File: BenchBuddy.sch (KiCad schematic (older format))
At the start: 0 parts

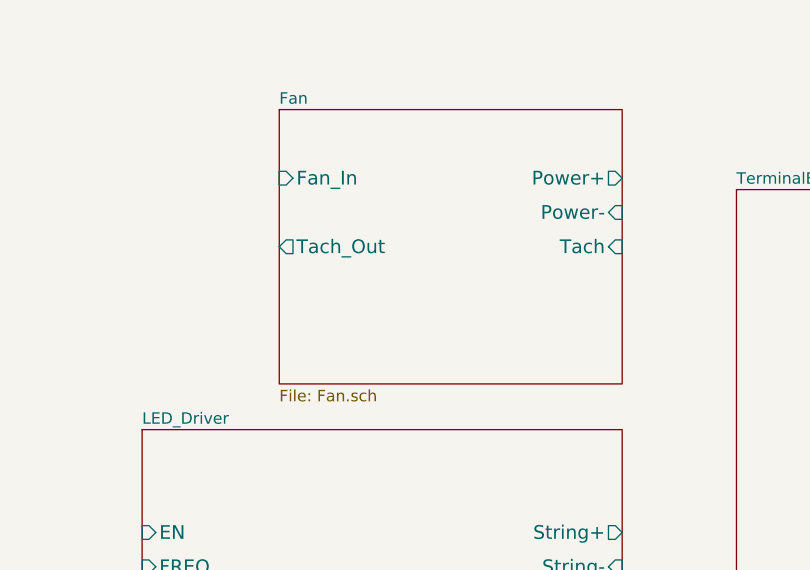
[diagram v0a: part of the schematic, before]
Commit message: Fan Schematic
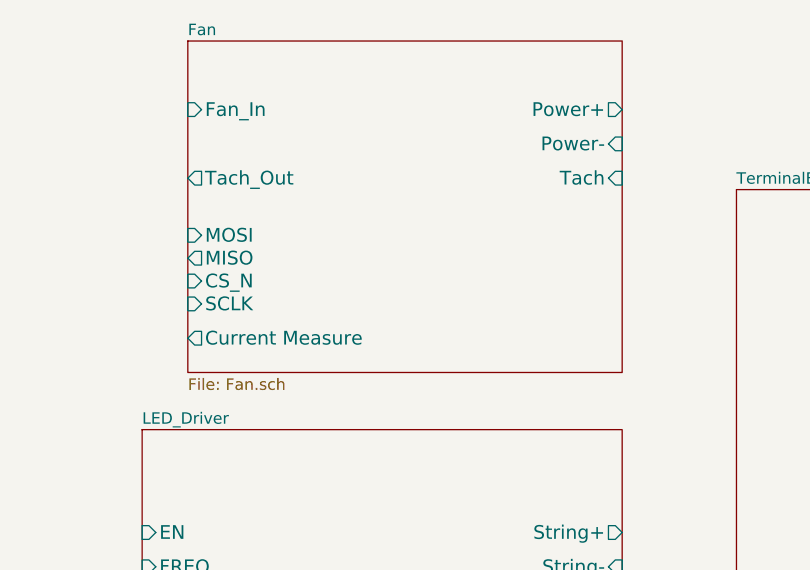
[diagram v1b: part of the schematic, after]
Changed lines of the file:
@@
 Sheet 1 8
 Title ""
-Date "19 sep 2013"
+Date "20 sep 2013"
 Rev ""
 Comp ""
@@
 $EndSheet
 $Sheet
-S 8250 1100 1500 1200
+S 7850 800  1900 1450
 U 5237E1FA
 F0 "Fan" 50
 F1 "Fan.sch" 50
-F2 "Fan_In" I L 8250 1400 60
-F3 "Tach_Out" O L 8250 1700 60
-F4 "Power+" O R 9750 1400 60
-F5 "Power-" I R 9750 1550 60
-F6 "Tach" I R 9750 1700 60
+F2 "Fan_In" I L 7850 1100 60
+F3 "Tach_Out" O L 7850 1400 60
+F4 "Power+" O R 9750 1100 60
+F5 "Power-" I R 9750 1250 60
+F6 "Tach" I R 9750 1400 60
+F7 "MOSI" I L 7850 1650 60
+F8 "MISO" O L 7850 1750 60
+F9 "CS_N" I L 7850 1850 60
+F10 "SCLK" I L 7850 1950 60
+F11 "Current Measure" O L 7850 2100 60
 $EndSheet
 $Sheet

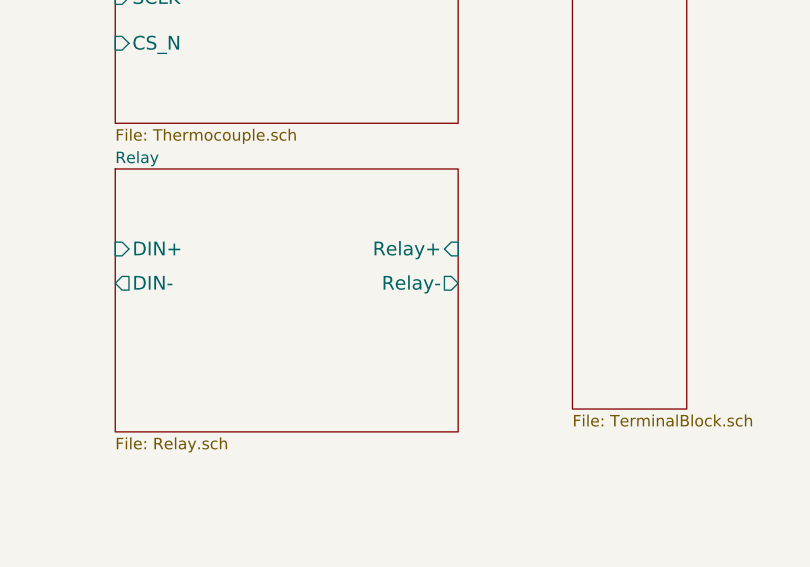
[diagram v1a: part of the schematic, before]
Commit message: Relay Schematic
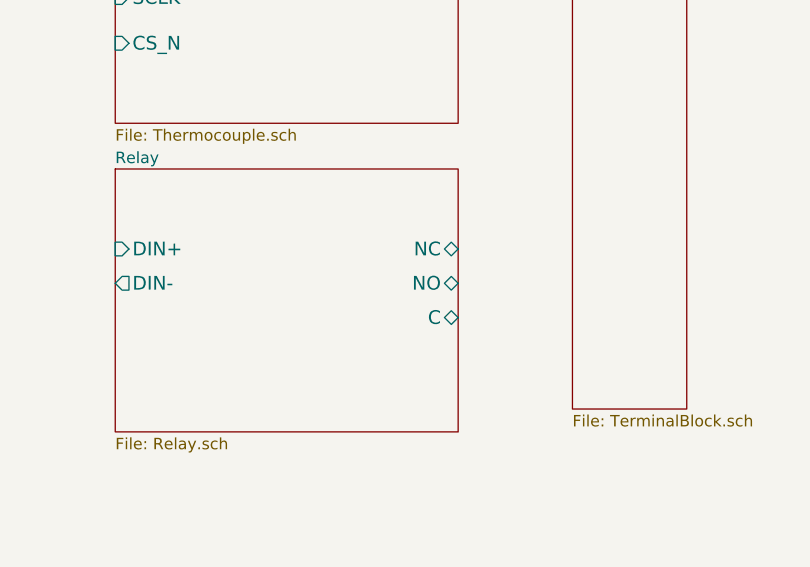
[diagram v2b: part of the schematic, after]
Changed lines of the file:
@@
 LIBS:contrib
 LIBS:valves
+LIBS:BenchBuddy
 LIBS:BenchBuddy-cache
 EELAYER 27 0
@@
 Sheet 1 8
 Title ""
-Date "20 sep 2013"
+Date "21 sep 2013"
 Rev ""
 Comp ""
@@
 F6 "SCLK" I L 8250 4950 60
 F7 "CS_N" I L 8250 5150 60
-$EndSheet
-$Sheet
-S 8250 5700 1500 1150
-U 5237E13C
-F0 "Relay" 50
-F1 "Relay.sch" 50
-F2 "DIN+" I L 8250 6050 60
-F3 "DIN-" O L 8250 6200 60
-F4 "Relay+" I R 9750 6050 60
-F5 "Relay-" O R 9750 6200 60
 $EndSheet
 $Sheet
@@
 F1 "TerminalBlock.sch" 50
 $EndSheet
+$Sheet
+S 8250 5700 1500 1150
+U 5237E13C
+F0 "Relay" 50
+F1 "Relay.sch" 50
+F2 "DIN+" I L 8250 6050 60
+F3 "DIN-" O L 8250 6200 60
+F6 "NC" B R 9750 6050 60
+F7 "NO" B R 9750 6200 60
+F8 "C" B R 9750 6350 60
+$EndSheet
 $EndSCHEMATC

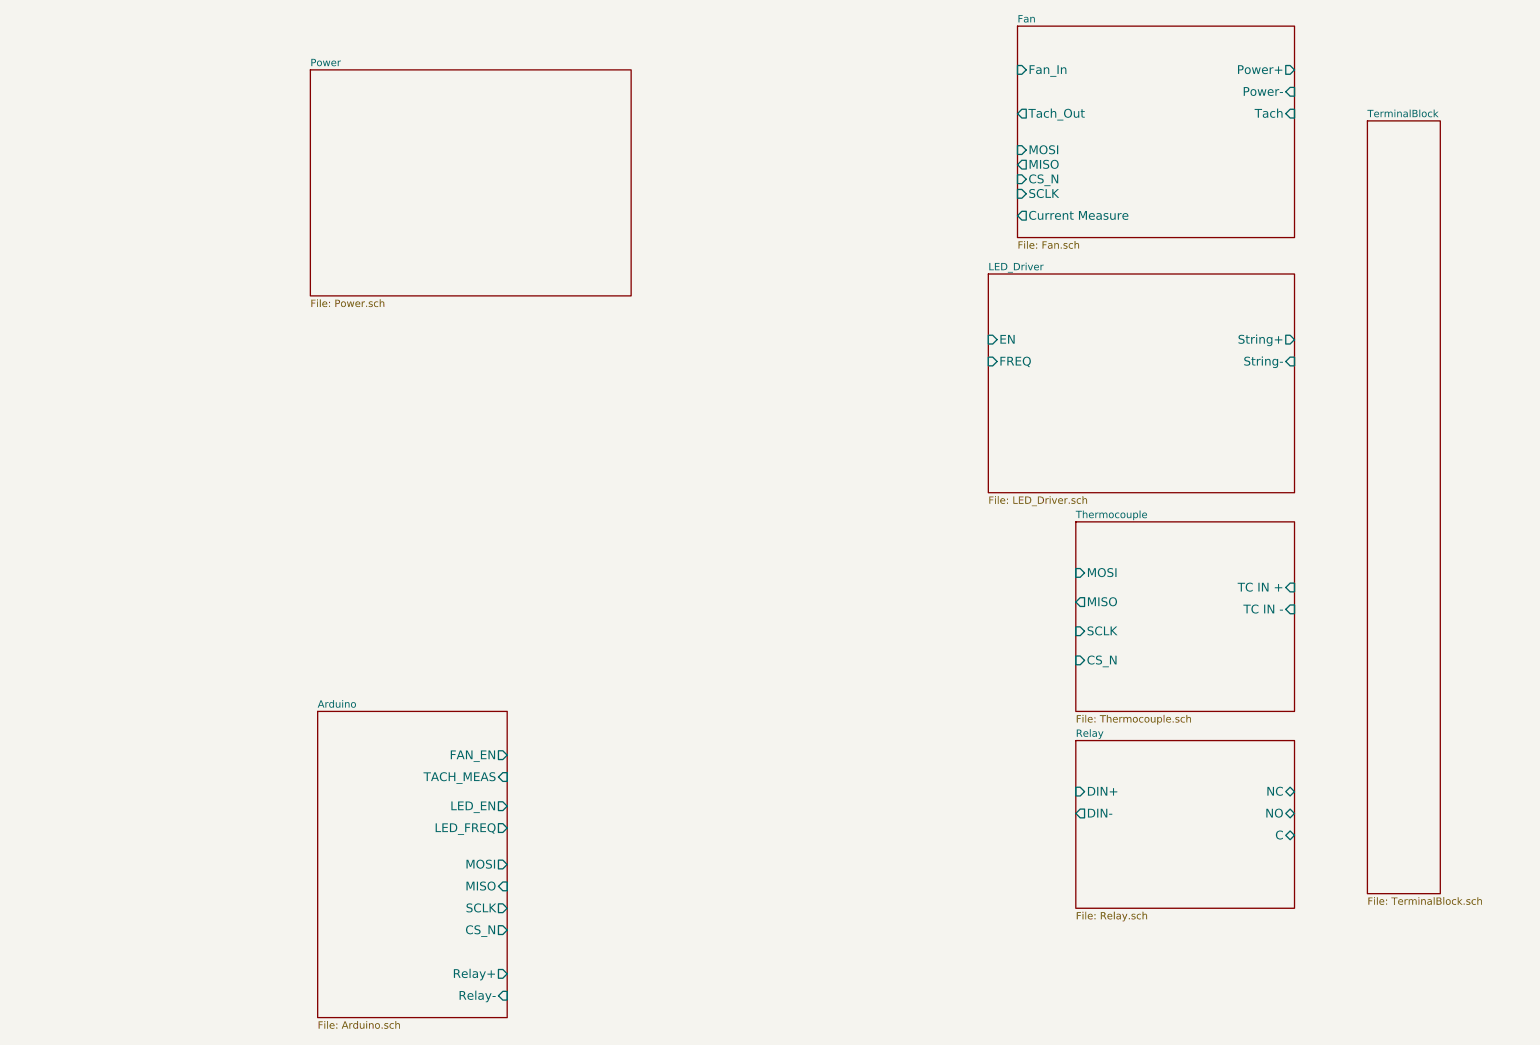
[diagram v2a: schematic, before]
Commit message: Power Protection And Filtering
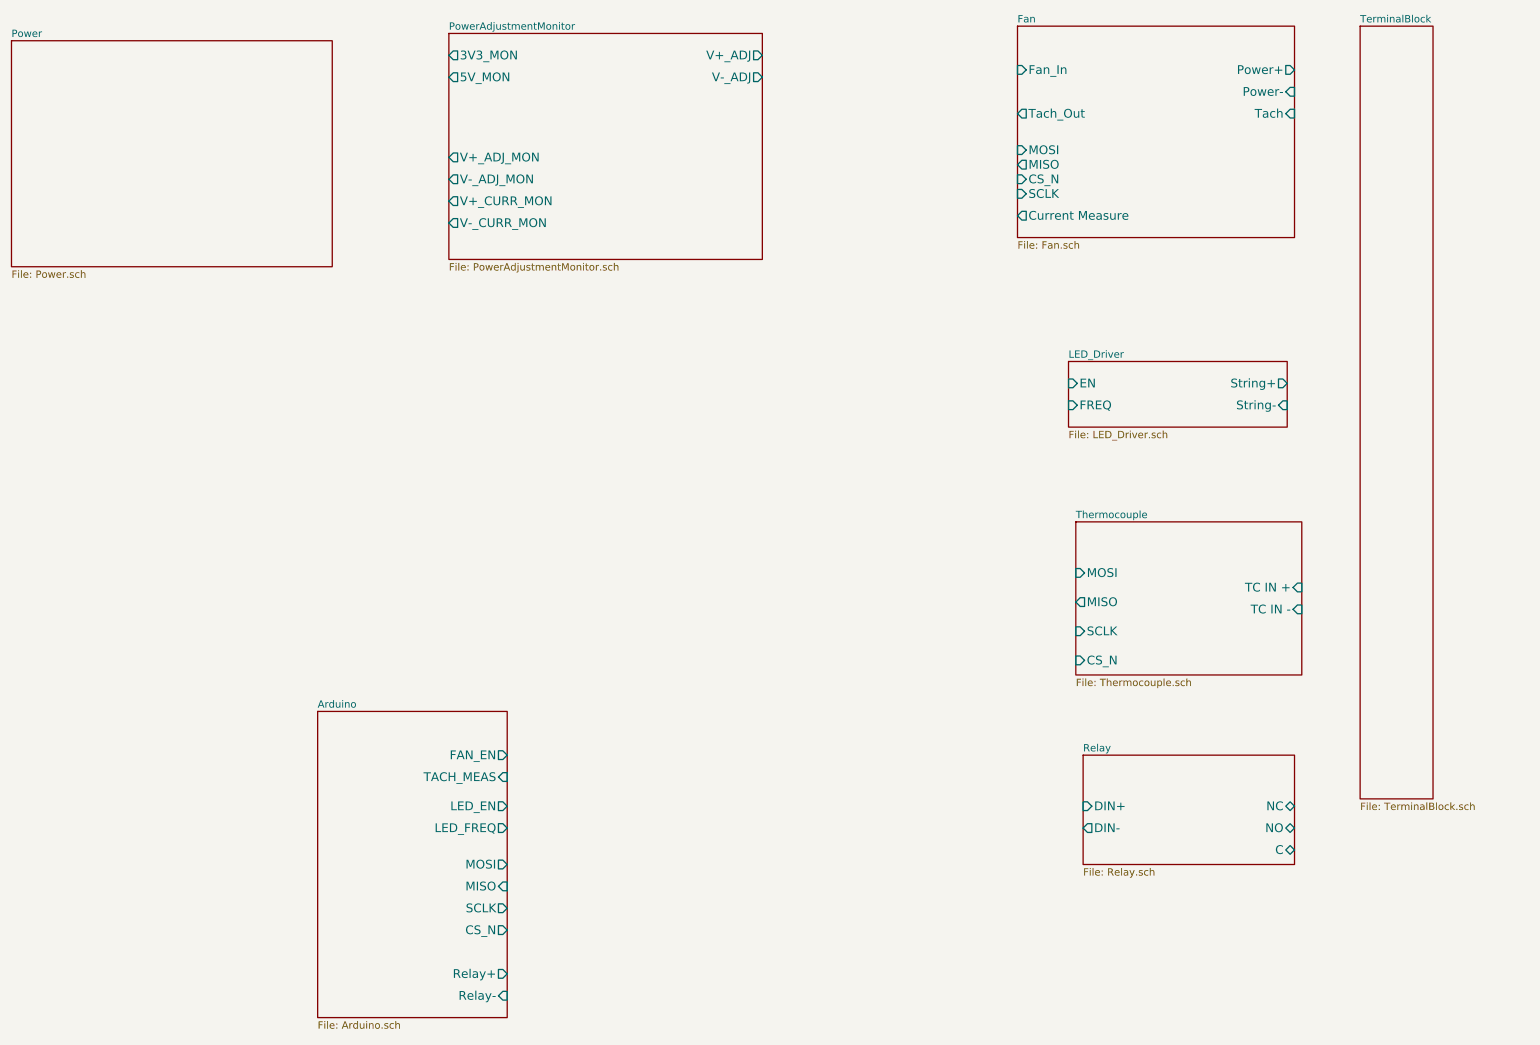
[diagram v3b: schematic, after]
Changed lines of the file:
@@
 $Descr A4 11693 8268
 encoding utf-8
-Sheet 1 8
+Sheet 1 9
 Title ""
-Date "21 sep 2013"
+Date "22 sep 2013"
 Rev ""
 Comp ""
@@
 $EndSheet
 $Sheet
-S 8250 4200 1500 1300
+S 8250 4200 1550 1050
 U 5237E11D
 F0 "Thermocouple" 50
 F1 "Thermocouple.sch" 50
-F2 "TC IN +" I R 9750 4650 60
-F3 "TC IN -" I R 9750 4800 60
+F2 "TC IN +" I R 9800 4650 60
+F3 "TC IN -" I R 9800 4800 60
 F4 "MOSI" I L 8250 4550 60
 F5 "MISO" O L 8250 4750 60
@@
 $EndSheet
 $Sheet
-S 3000 1100 2200 1550
+S 950  900  2200 1550
 U 5237E175
 F0 "Power" 50
@@
 $EndSheet
 $Sheet
-S 7650 2500 2100 1500
+S 8200 3100 1500 450
 U 5237E1C9
 F0 "LED_Driver" 50
 F1 "LED_Driver.sch" 50
-F2 "EN" I L 7650 2950 60
-F3 "FREQ" I L 7650 3100 60
-F4 "String+" O R 9750 2950 60
-F5 "String-" I R 9750 3100 60
+F2 "EN" I L 8200 3250 60
+F3 "FREQ" I L 8200 3400 60
+F4 "String+" O R 9700 3250 60
+F5 "String-" I R 9700 3400 60
 $EndSheet
 $Sheet
@@
 $EndSheet
 $Sheet
-S 10250 1450 500  5300
+S 10200 800  500  5300
 U 5237E269
 F0 "TerminalBlock" 50
@@
 $EndSheet
 $Sheet
-S 8250 5700 1500 1150
+S 8300 5800 1450 750
 U 5237E13C
 F0 "Relay" 50
 F1 "Relay.sch" 50
-F2 "DIN+" I L 8250 6050 60
-F3 "DIN-" O L 8250 6200 60
-F6 "NC" B R 9750 6050 60
-F7 "NO" B R 9750 6200 60
-F8 "C" B R 9750 6350 60
+F2 "DIN+" I L 8300 6150 60
+F3 "DIN-" O L 8300 6300 60
+F4 "NC" B R 9750 6150 60
+F5 "NO" B R 9750 6300 60
+F6 "C" B R 9750 6450 60
+$EndSheet
+$Sheet
+S 3950 850  2150 1550
+U 523E68DB
+F0 "PowerAdjustmentMonitor" 50
+F1 "PowerAdjustmentMonitor.sch" 50
+F2 "V+_ADJ" O R 6100 1000 60
+F3 "V-_ADJ" O R 6100 1150 60
+F4 "3V3_MON" O L 3950 1000 60
+F5 "5V_MON" O L 3950 1150 60
+F6 "V+_ADJ_MON" O L 3950 1700 60
+F7 "V-_ADJ_MON" O L 3950 1850 60
+F8 "V+_CURR_MON" O L 3950 2000 60
+F9 "V-_CURR_MON" O L 3950 2150 60
 $EndSheet
 $EndSCHEMATC

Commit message: Overall Schematic
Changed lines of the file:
@@
 Sheet 1 9
 Title ""
-Date "22 sep 2013"
+Date "28 sep 2013"
 Rev ""
 Comp ""
@@
 $EndDescr
 $Sheet
-S 3050 5500 1300 2100
-U 5237E014
-F0 "Arduino" 50
-F1 "Arduino.sch" 50
-F2 "FAN_EN" O R 4350 5800 60
-F3 "TACH_MEAS" I R 4350 5950 60
-F4 "LED_EN" O R 4350 6150 60
-F5 "LED_FREQ" O R 4350 6300 60
-F6 "MOSI" O R 4350 6550 60
-F7 "MISO" I R 4350 6700 60
-F8 "SCLK" O R 4350 6850 60
-F9 "CS_N" O R 4350 7000 60
-F10 "Relay+" O R 4350 7300 60
-F11 "Relay-" I R 4350 7450 60
-$EndSheet
-$Sheet
-S 8250 4200 1550 1050
+S 8200 2950 1550 1050
 U 5237E11D
 F0 "Thermocouple" 50
 F1 "Thermocouple.sch" 50
-F2 "TC IN +" I R 9800 4650 60
-F3 "TC IN -" I R 9800 4800 60
-F4 "MOSI" I L 8250 4550 60
-F5 "MISO" O L 8250 4750 60
-F6 "SCLK" I L 8250 4950 60
-F7 "CS_N" I L 8250 5150 60
+F2 "TC IN +" I R 9750 3400 60
+F3 "TC IN -" I R 9750 3550 60
+F4 "MOSI" I L 8200 3300 60
+F5 "MISO" O L 8200 3400 60
+F6 "SCLK" I L 8200 3500 60
+F7 "CS_N" I L 8200 3600 60
 $EndSheet
 $Sheet
@@
 $EndSheet
 $Sheet
-S 8200 3100 1500 450
+S 8250 4400 1500 450
 U 5237E1C9
 F0 "LED_Driver" 50
 F1 "LED_Driver.sch" 50
-F2 "EN" I L 8200 3250 60
-F3 "FREQ" I L 8200 3400 60
-F4 "String+" O R 9700 3250 60
-F5 "String-" I R 9700 3400 60
-$EndSheet
-$Sheet
-S 7850 800  1900 1450
+F2 "LED_EN_PWM" I L 8250 4600 60
+F3 "LED_STRING+" O R 9750 4550 60
+F4 "LED_STRING-" O R 9750 4700 60
+$EndSheet
+$Sheet
+S 7850 1100 1900 1450
 U 5237E1FA
 F0 "Fan" 50
 F1 "Fan.sch" 50
-F2 "Fan_In" I L 7850 1100 60
-F3 "Tach_Out" O L 7850 1400 60
-F4 "Power+" O R 9750 1100 60
-F5 "Power-" I R 9750 1250 60
-F6 "Tach" I R 9750 1400 60
-F7 "MOSI" I L 7850 1650 60
-F8 "MISO" O L 7850 1750 60
-F9 "CS_N" I L 7850 1850 60
-F10 "SCLK" I L 7850 1950 60
-F11 "Current Measure" O L 7850 2100 60
-$EndSheet
-$Sheet
-S 10200 800  500  5300
+F2 "MOSI" I L 7850 1550 60
+F3 "MISO" O L 7850 1650 60
+F4 "CS_N" I L 7850 1750 60
+F5 "SCLK" I L 7850 1850 60
+F6 "FAN_EN_N" I L 7850 1250 60
+F7 "TACH_MEAS" O L 7850 2200 60
+F8 "FAN_OUT+" O R 9750 1350 60
+F9 "FAN_OUT-" O R 9750 1500 60
+F10 "TACH_IN" I R 9750 2300 60
+F11 "CURR_MEAS" O L 7850 2300 60
+$EndSheet
+$Sheet
+S 8250 5550 1450 750
+U 5237E13C
+F0 "Relay" 50
+F1 "Relay.sch" 50
+F2 "RELAY+" I L 8250 5800 60
+F3 "RELAY-" O L 8250 6000 60
+F4 "RELAY_NC" B R 9700 5900 60
+F5 "RELAY_NO" B R 9700 5800 60
+F6 "RELAY_COM" B R 9700 5700 60
+$EndSheet
+$Sheet
+S 4950 800  2050 1450
+U 523E68DB
+F0 "PowerAdjustmentMonitor" 50
+F1 "PowerAdjustmentMonitor.sch" 50
+F2 "V+_ADJ" O R 7000 900 60
+F3 "V-_ADJ" O R 7000 1000 60
+F4 "3V3_MON" O L 4950 950 60
+F5 "5V_MON" O L 4950 1100 60
+F6 "V+_ADJ_MON" O L 4950 1950 60
+F7 "V-_ADJ_MON" O L 4950 2100 60
+F8 "V+_CURR_MON" O L 4950 1350 60
+F9 "V-_CURR_MON" O L 4950 1500 60
+$EndSheet
+Wire Wire Line
+	4050 4100 4400 4100
+Wire Wire Line
+	4400 4100 4400 1950
+Wire Wire Line
+	4400 1950 4950 1950
+Wire Wire Line
+	4950 2100 4500 2100
+Wire Wire Line
+	4500 2100 4500 4200
+Wire Wire Line
+	4500 4200 4050 4200
+Wire Wire Line
+	4050 4350 7150 4350
+Wire Wire Line
+	7150 4350 7150 1250
+Wire Wire Line
+	7150 1250 7850 1250
+Wire Wire Line
+	7850 1550 7200 1550
+Wire Wire Line
+	7200 1550 7200 4500
+Wire Wire Line
+	7200 4500 4050 4500
+Wire Wire Line
+	4050 4600 7250 4600
+Wire Wire Line
+	7250 4600 7250 1650
+Wire Wire Line
+	7250 1650 7850 1650
+Wire Wire Line
+	7850 1750 7300 1750
+Wire Wire Line
+	7300 1750 7300 4700
+Wire Wire Line
+	7300 4700 4050 4700
+Wire Wire Line
+	4050 4800 7350 4800
+Wire Wire Line
+	7350 4800 7350 1850
+Wire Wire Line
+	7350 1850 7850 1850
+Wire Wire Line
+	7850 2200 7400 2200
+Wire Wire Line
+	7400 2200 7400 4950
+Wire Wire Line
+	7400 4950 4050 4950
+Wire Wire Line
+	4050 5050 7450 5050
+Wire Wire Line
+	7450 5050 7450 2300
+Wire Wire Line
+	7450 2300 7850 2300
+Wire Wire Line
+	8200 3300 7200 3300
+Connection ~ 7200 3300
+Wire Wire Line
+	8200 3400 7250 3400
+Connection ~ 7250 3400
+$Sheet
+S 2750 4000 1300 2100
+U 5237E014
+F0 "Arduino" 50
+F1 "Arduino.sch" 50
+F2 "TACH_MEAS" I R 4050 4950 60
+F3 "MOSI" O R 4050 4500 60
+F4 "MISO" I R 4050 4600 60
+F5 "SCLK" O R 4050 4800 60
+F6 "FAN_EN_N" O R 4050 4350 60
+F7 "CURR_MEAS" I R 4050 5050 60
+F8 "RELAY+" O R 4050 5800 60
+F9 "RELAY-" O R 4050 6000 60
+F10 "V+_ADJ_MON" I R 4050 4100 60
+F11 "V-_ADJ_MON" I R 4050 4200 60
+F12 "LED_EN_PWM" O R 4050 5300 60
+F13 "DAC_CS_N" O R 4050 4700 60
+F14 "ADC_CS_N" O R 4050 5150 60
+$EndSheet
+Wire Wire Line
+	7350 3500 8200 3500
+Connection ~ 7350 3500
+Wire Wire Line
+	8200 3600 7500 3600
+Wire Wire Line
+	7500 3600 7500 5150
+Wire Wire Line
+	7500 5150 4050 5150
+Wire Wire Line
+	4050 5300 7700 5300
+Wire Wire Line
+	7700 5300 7700 4600
+Wire Wire Line
+	7700 4600 8250 4600
+Wire Wire Line
+	4050 5800 8250 5800
+Wire Wire Line
+	8250 6000 4050 6000
+$Sheet
+S 10250 800  750  5500
 U 5237E269
 F0 "TerminalBlock" 50
 F1 "TerminalBlock.sch" 50
-$EndSheet
-$Sheet
-S 8300 5800 1450 750
-U 5237E13C
-F0 "Relay" 50
-F1 "Relay.sch" 50
-F2 "DIN+" I L 8300 6150 60
-F3 "DIN-" O L 8300 6300 60
-F4 "NC" B R 9750 6150 60
-F5 "NO" B R 9750 6300 60
-F6 "C" B R 9750 6450 60
-$EndSheet
-$Sheet
-S 3950 850  2150 1550
-U 523E68DB
-F0 "PowerAdjustmentMonitor" 50
-F1 "PowerAdjustmentMonitor.sch" 50
-F2 "V+_ADJ" O R 6100 1000 60
-F3 "V-_ADJ" O R 6100 1150 60
-F4 "3V3_MON" O L 3950 1000 60
-F5 "5V_MON" O L 3950 1150 60
-F6 "V+_ADJ_MON" O L 3950 1700 60
-F7 "V-_ADJ_MON" O L 3950 1850 60
-F8 "V+_CURR_MON" O L 3950 2000 60
-F9 "V-_CURR_MON" O L 3950 2150 60
-$EndSheet
+F2 "V+_ADJ" I L 10250 900 60
+F3 "V-_ADJ" I L 10250 1000 60
+F4 "FAN_OUT+" O L 10250 1350 60
+F5 "FAN_OUT-" O L 10250 1500 60
+F6 "TACH_IN" I L 10250 2300 60
+F7 "TC_IN+" I L 10250 3400 60
+F8 "TC_IN-" I L 10250 3550 60
+F9 "LED_STRING+" O L 10250 4550 60
+F10 "LED_STRING-" O L 10250 4700 60
+F11 "RELAY_COM" B L 10250 5700 60
+F12 "RELAY_NO" B L 10250 5800 60
+F13 "RELAY_NC" B L 10250 5900 60
+$EndSheet
+Wire Wire Line
+	7000 900  10250 900
+Wire Wire Line
+	7000 1000 10250 1000
+Wire Wire Line
+	9750 1350 10250 1350
+Wire Wire Line
+	9750 1500 10250 1500
+Wire Wire Line
+	9750 2300 10250 2300
+Wire Wire Line
+	9750 3400 10250 3400
+Wire Wire Line
+	9750 3550 10250 3550
+Wire Wire Line
+	9750 4550 10250 4550
+Wire Wire Line
+	9750 4700 10250 4700
+Wire Wire Line
+	9700 5700 10250 5700
+Wire Wire Line
+	9700 5800 10250 5800
+Wire Wire Line
+	9700 5900 10250 5900
 $EndSCHEMATC
